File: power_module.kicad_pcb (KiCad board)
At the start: 4 copper layers, 95 x 76.9 mm, 71 parts, among them J1 USB_C_PD, J2 OUTPUT, J3 I2C_BREAKOUT, Q1 DUAL_N_FET, Q2 DUAL_N_FET, Q3 DUAL_N_FET, Q4 DUAL_N_FET, SW1 ON_OFF, U1 BQ7692003, U2 CH224K, U3 BQ24650, U4 LM5176PWPR

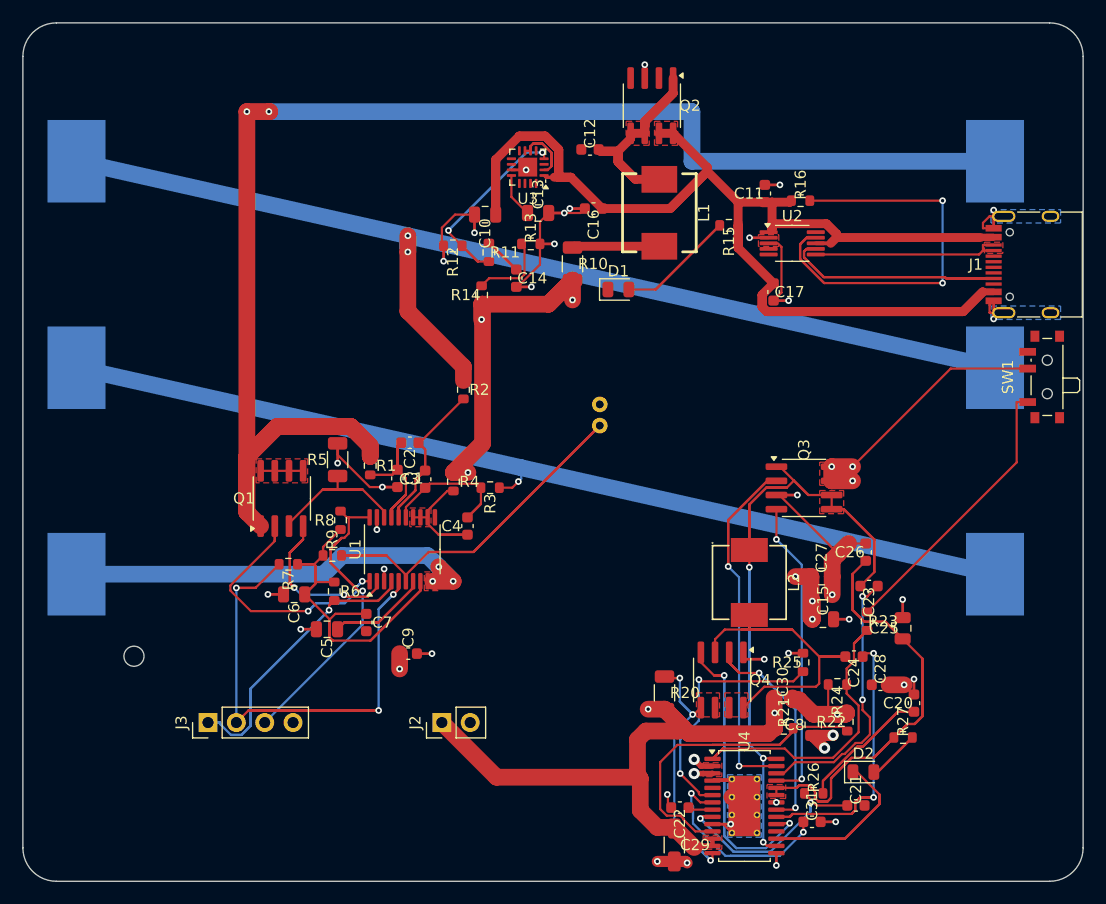
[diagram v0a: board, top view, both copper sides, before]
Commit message: dedupe: remove 201 exact-duplicate tracks left by autoroute re-imports
Result of running dedupe_traces(apply=true) on the board. The duplicates
were accumulated over the stop-and-go routing sessions where autoroute /
import_ses ran more than once — pcbnew.ImportSpecctraSES appends rather
than replaces, so each rerun left a clone of every routed segment on
top of the previous one.

KiCAD-MCP-Server commit ce7a3a2 now calls dedupe_traces automatically
at the end of autoroute and import_ses, so this kind of accumulation
won't happen again in future sessions.

DRC: doubled-trace-induced noise cleared. Down from ~250 to 34 total
violations (28 errors, 6 warnings); much closer to a real picture of
what still needs fixing.

Co-Authored-By: Claude Opus 4.7 <noreply@anthropic.com>
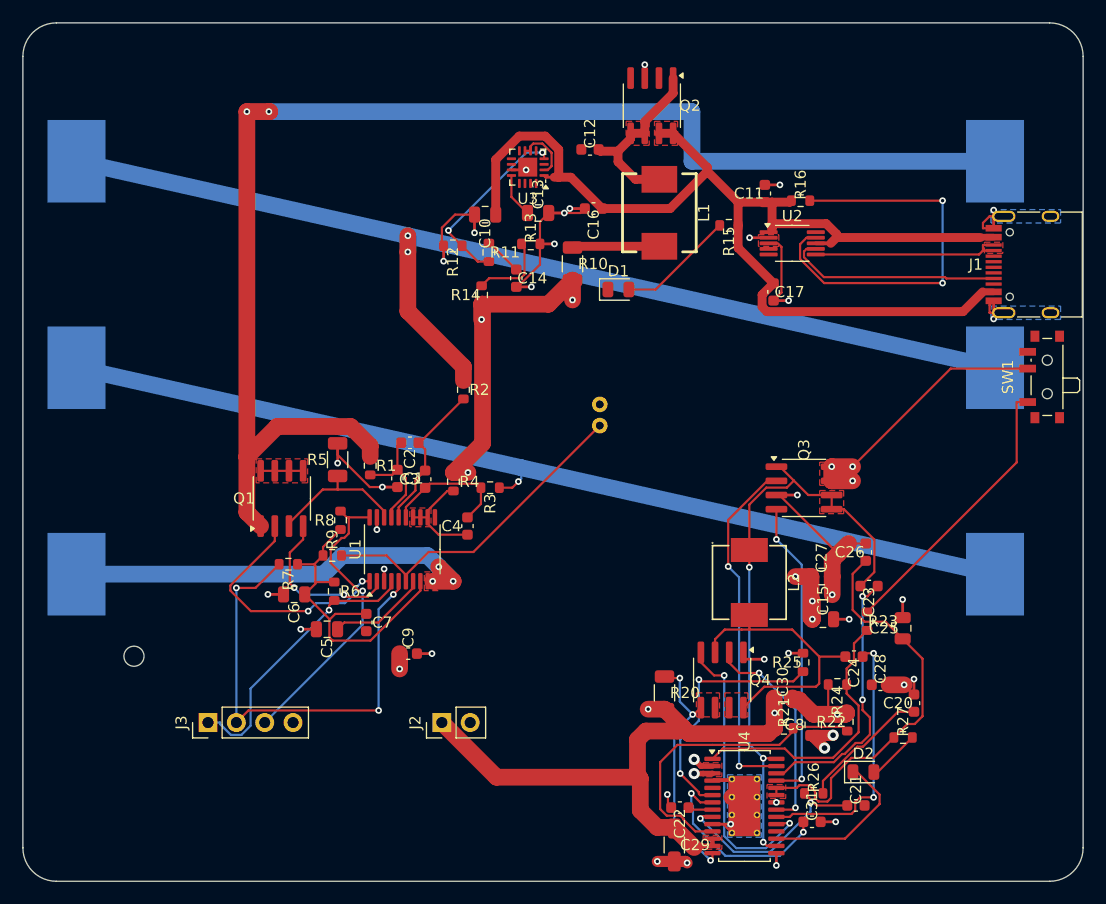
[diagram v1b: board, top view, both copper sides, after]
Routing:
- net USB_VBUS: track 150.1 -> 104.6 mm
- net BB_SW1: track 89.9 -> 55.1 mm
- net BB_VCC: track 67.6 -> 37.1 mm
- net TS1: track 54.0 -> 30.0 mm
- net SDA: track 48.1 -> 25.2 mm
- net BAT-: track 143.8 -> 125.0 mm
- net CC1: track 38.1 -> 19.4 mm
- net BB_HDRV2: track 44.4 -> 26.4 mm
- net REGOUT: track 46.7 -> 29.7 mm
- net SCL: track 58.2 -> 42.3 mm
- net BQ_TS: track 28.8 -> 16.8 mm
- net BB_PGOOD: track 26.4 -> 14.6 mm
- net BB_COMPMID: track 22.2 -> 11.8 mm
- net BQ_PH: track 26.3 -> 16.4 mm
- net BB_HDRV1: track 40.7 -> 31.6 mm
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
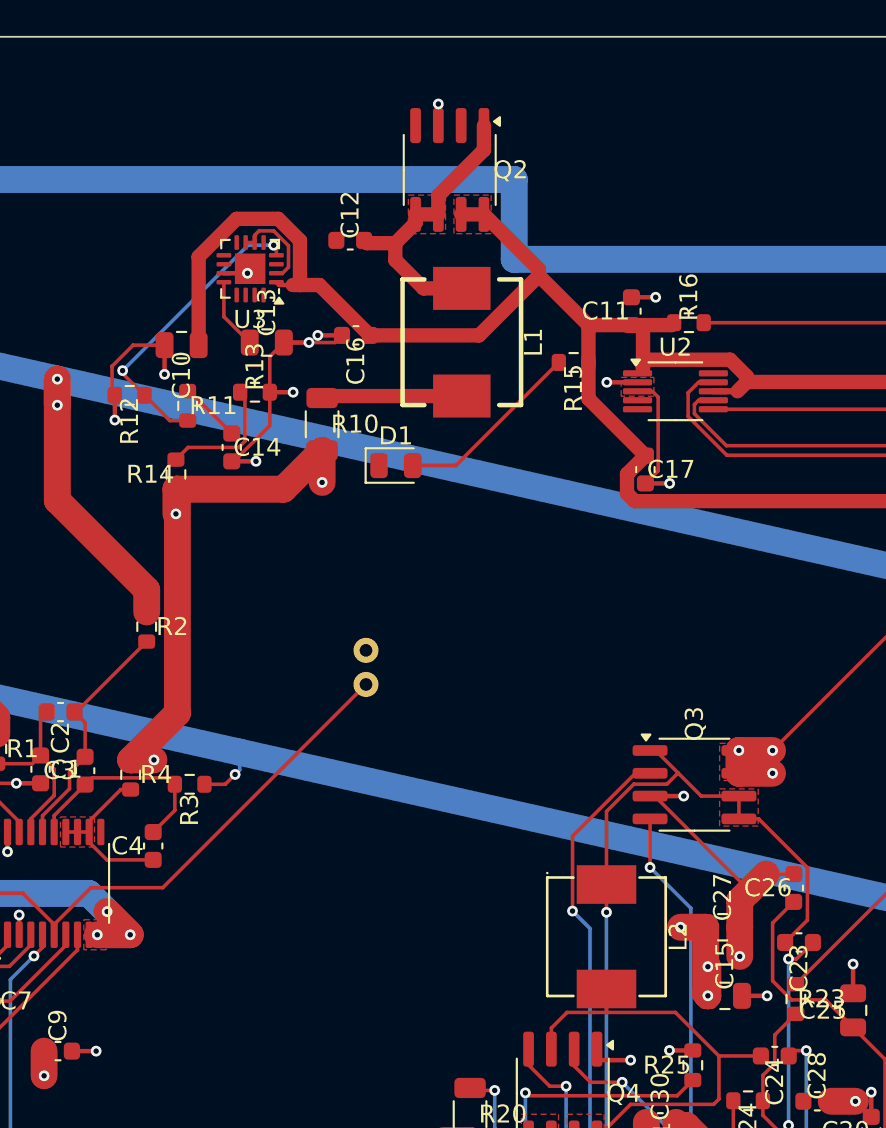
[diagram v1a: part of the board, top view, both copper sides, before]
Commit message: charger: per-target spring annotations + selective autoplace of U3 group
Annotate U3's decoupling/bulk/bootstrap caps with per-target
Pin_Spring_Class ({"U3.N": "DECOUPLING"}) so each is pulled onto the
specific pin it serves rather than everything on its rail; status LED
D1 weakly tethered (INTER_GROUP). Classify USB_VBUS as INTER_GROUP in
the META1 spring-class net map (cross-group rail; stops Q2 drifting to
the input side). Selectively relax the charger satellites with U3
anchored and all other groups locked.

Co-Authored-By: Claude Opus 4.7 <noreply@anthropic.com>
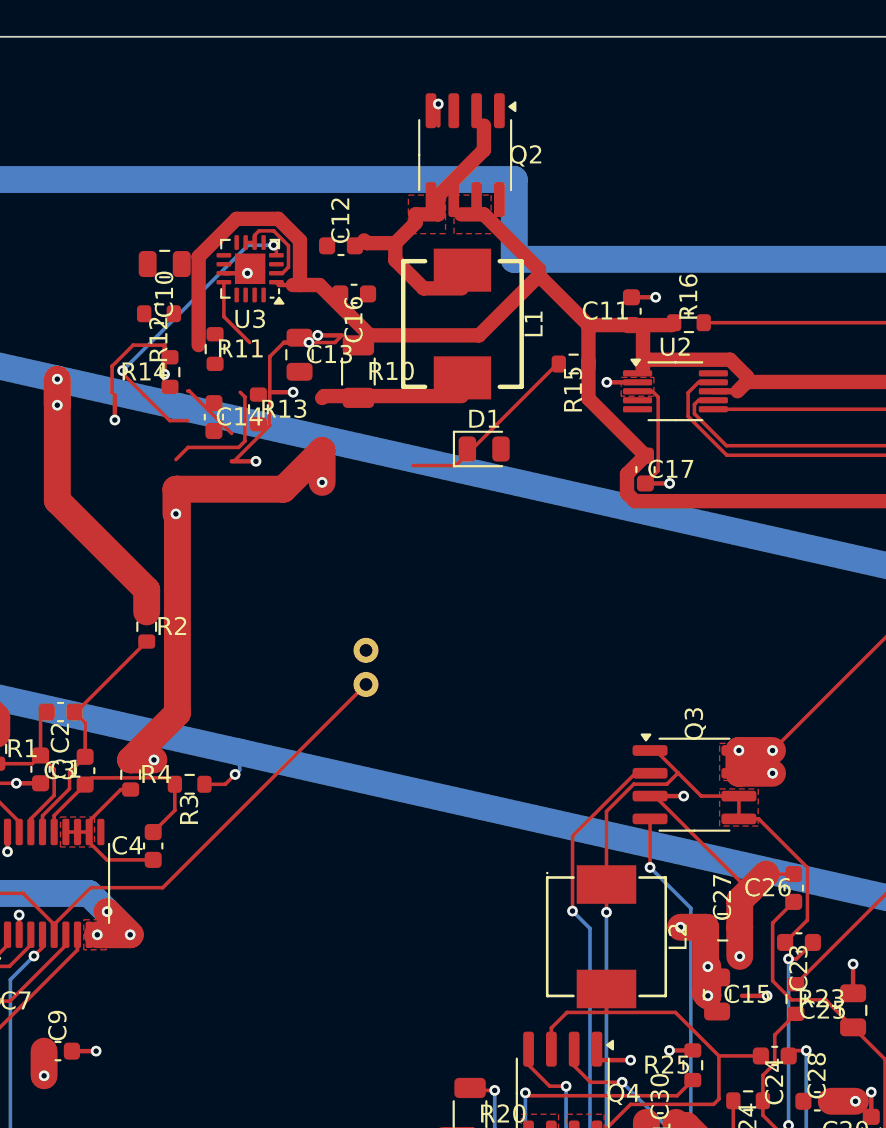
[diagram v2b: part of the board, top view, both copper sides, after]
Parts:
- moved R14 5.71 mm to (40.8, 18.7)
- moved D1 5.01 mm to (58.3, 23.0)
- moved R12 4.83 mm to (40.2, 15.5)
- moved C10 4.62 mm to (40.5, 12.7)
- moved R10 3.57 mm to (51.3, 18.7)
- moved R11 3.51 mm to (43.3, 17.4)
- moved C16 2.31 mm to (51.1, 14.4)
- moved C14 1.96 mm to (43.3, 21.2)
- moved C13 1.95 mm to (48.0, 17.8), turned to -90 degrees
- moved Q2 1.19 mm to (57.3, 6.64)
- moved L1 1.02 mm to (57.1, 16.1)
- moved R13 0.98 mm to (45.7, 20.8), turned to -90 degrees
- moved C12 0.60 mm to (50.3, 11.7)
- moved C15 0.44 mm to (71.3, 53.4), turned to -90 degrees
- moved R15 0.09 mm to (63.3, 18.3)
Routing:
- net GND: track 116.3 -> 107.0 mm, vias 36 -> 33
- net BQ_VFB: track 7.11 -> 15.2 mm, vias 0 -> 2
- net BQ_LODRV: track 0.00 -> 1.20 mm, vias 0 -> 1
